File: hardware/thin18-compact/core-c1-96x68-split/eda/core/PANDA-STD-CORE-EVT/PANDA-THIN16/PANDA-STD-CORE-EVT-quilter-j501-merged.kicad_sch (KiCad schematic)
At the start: 126 parts, among them J301 DF58-2P-1.2V(21), J501 104031-0811 / microSD, J502 SM02B-SRSS-TB, J503 TC2030-IDC-NL / DEBUG, J803 FH34SRJ-6S-0.5SH(50), SW201 SKSCLCE010, SW202 SKSCLCE010, U301 BQ27427YZFR, U302 RV-3028-C7, U402 TPS22916CYFPT, U403 TPS22916CYFPT, U404 TPS22916CYFPT, U405 TPS22916CYFPT, U501 ESP32-S3-WROOM-1U-N16R8, U502 MAX98357AETE+T, U503 QMI8658A, U601 XL9535, U901 SGM41513YTQF24G/TR, U902 SGM62125AXG/TR, U903 CW2217BAAD, U904 NS4168

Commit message: feat(hw): audit split stack and verify exact-part sourcing
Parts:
- J301: LCSC (none) -> C597951
- J501: LCSC (none) -> C585350
- R306: LCSC (none) -> C7467248
- R903, R904: LCSC (none) -> C2906981
- U501: LCSC (none) -> C3013946
- U903: LCSC (none) -> C5203993

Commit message: hw: correct prototype footprints and prepare Split-C1 JLC CAM handoff
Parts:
- C506, C513: LCSC (none) -> C22399626; MPN 0603B106K100NT -> CGA0603X7R106K100JT; Manufacturer FH (Fenghua Advanced) -> HRE
- L402: footprint panda-standard:L402_2U2_ENVELOPE -> panda-standard:XGL4015_Coilcraft

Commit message: hw: apply reviewed domestic ECOs and gate incomplete Split-C1 orders
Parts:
- added C516: 1u / U403 VOUT, Capacitor_SMD:C_0603_1608Metric, symbol Device:C
- R201: LCSC C23189 -> C99891; MPN 0603WAF5601T5E -> RS-03K5601FT; Manufacturer UNI-ROYAL -> FH (Fenghua Advanced)
- R204: LCSC C22765 -> C118396; MPN 0603WAF1201T5E -> RS-03K1201FT; Manufacturer UNI-ROYAL -> FH (Fenghua Advanced)
- R303, R510, R511, R512, R513, R523, R524, R525, R526, R527, R528, R600: LCSC C25744 -> C140215; MPN 0402WGF1002TCE -> RC-02K1002FT; Manufacturer UNI-ROYAL -> FH (Fenghua Advanced)
- R501, R502, R507, R604, R605, R606, R607, R608, R609, R610, R611, R612: LCSC C25741 -> C140219; MPN 0402WGF1003TCE -> RC-02K1003FT; Manufacturer UNI-ROYAL -> FH (Fenghua Advanced)
- R508, R509, R514, R515, R516: LCSC C17477 -> C132364; MPN 0805W8F0000T5E -> RS-05000FT; Manufacturer UNI-ROYAL -> FH (Fenghua Advanced)
- R517, R518, R519, R520, R521, R522: LCSC C21189 -> C136582; MPN 0603WAF0000T5E -> RS-03000FT; Manufacturer UNI-ROYAL -> FH (Fenghua Advanced)
- R613, R614: LCSC C25879 -> C140192; MPN 0402WGF2201TCE -> RC-02K2201FT; Manufacturer UNI-ROYAL -> FH (Fenghua Advanced)
- U402, U403, U404, U405: value TPS22916CYFPT -> SGM2578SDYG/TR; footprint panda-standard:TPS22916CYFPT_YFP0004 -> panda-standard:SGM2578SD_WLCSP_09x09_P05; symbol panda-standard:TPS22916CYFPT -> panda-standard:SGM2578SDYG_TR; LCSC C2680456 -> (none); MPN TPS22916CYFPT -> SGM2578SDYG/TR; Manufacturer Texas Instruments -> SGMICRO
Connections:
- net 3V3_TOUCH_SW: now also C516.1
- net GND: now also C516.2

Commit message: hw: apply domestic wire, FPC and inductor ECOs with replay guards
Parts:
- J502: value SM02B-SRSS-TB -> HC-1.0-2PWT BTL; footprint Connector_JST:JST_SH_SM02B-SRSS-TB_1x02-1MP_P1.00mm_Horizontal -> panda-standard:HCTL_HC10_2PWT; LCSC C160402 -> C2845361; MPN SM02B-SRSS-TB(LF)(SN) -> HC-1.0-2PWT; Manufacturer JST -> HCTL
- J803: value FH34SRJ-6S-0.5SH(50) -> X05A10H06G; footprint PandaDomestic:FH34SRJ-6S-0.5SH_50 -> panda-standard:XKB_X05A10H06G_A2; LCSC C224194 -> C528032; MPN FH34SRJ-6S-0.5SH(50) -> X05A10H06G; Manufacturer Hirose -> XKB Connection; Qualification Exact C224194 land pattern imported; FPC orientation and ph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 -> Manufacturer X05A10HXX p2 A2, ECN-P-2026011502 dated2026-01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
- L401: value 0.47uH / M0-PENDING -> 0.47uH / SGM62125; footprint panda-standard:L401_XFL4015_ENVELOPE -> panda-standard:Sunlord_MWSA0402_R47; LCSC C18221164 -> C6331050; MPN XFL4015-471MEC -> MWSA0402S-R47MT; Manufacturer Coilcraft -> Sunlord
- L402: value 2.2u / BQ buck -> 1uH / SGM41513 buck; footprint panda-standard:XGL4015_Coilcraft -> panda-standard:Sunlord_MWSA0402_1R0B01; MPN XGL4015-222MEC -> MWSA0402S-1R0MTB01; Manufacturer Coilcraft -> Sunlord

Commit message: hw: replace side buttons with XKB A1 no-post switches
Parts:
- SW201, SW202: value SKSCLCE010 -> TS-1186E-B-B; footprint panda-standard:SW_Alps_SKSCLCE010 -> panda-standard:XKB_TS1186E_BB_A1; LCSC C139799 -> C2885153; MPN SKSCLCE010 -> TS-1186E-B-B; Manufacturer ALPSALPINE -> XKB Connection

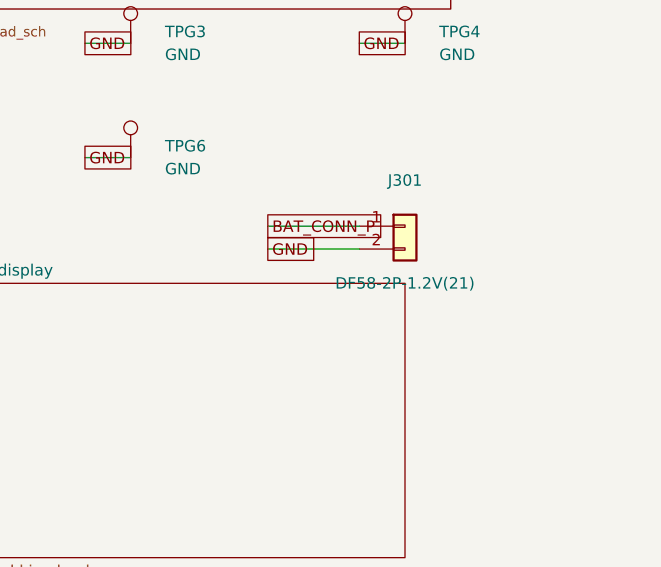
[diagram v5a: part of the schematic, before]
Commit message: hardware: close three imported Split-C1 refs and two SMT maps
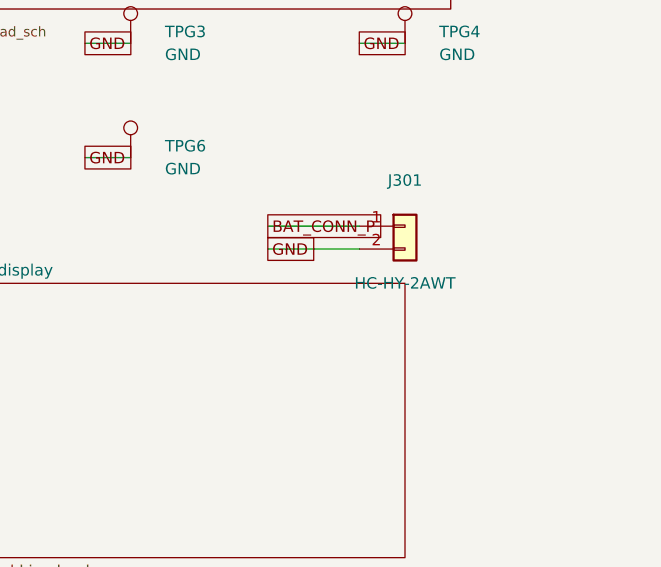
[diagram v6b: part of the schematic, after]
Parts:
- J301: value DF58-2P-1.2V(21) -> HC-HY-2AWT; footprint panda-battery:Hirose_DF58-2P-1.2V_1x02_P1.2mm_Vertical -> panda-standard:HCTL_HC_HY_2AWT; LCSC C597951 -> C2845705; MPN DF58-2P-1.2V(21) -> HC-HY-2AWT; Manufacturer Hirose -> HCTL

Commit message: hw: apply XUNPU microSD and reviewed Sunlord MT inductor ECOs
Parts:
- J501: value 104031-0811 / microSD -> TF-122-CCP9 / microSD; footprint Connector_Card:microSD_HC_Molex_104031-0811 -> panda-standard:XUNPU_TF_122_CCP9; symbol Connector:Micro_SD_Card_Det2 -> panda-standard:XUNPU_TF_122_CCP9; LCSC C585350 -> C41347844; MPN 104031-0811 -> TF-122-CCP9; Manufacturer Molex -> XUNPU
- L402: footprint panda-standard:Sunlord_MWSA0402_1R0B01 -> panda-standard:Sunlord_MWSA0402_1R0; LCSC (none) -> C408332; MPN MWSA0402S-1R0MTB01 -> MWSA0402S-1R0MT

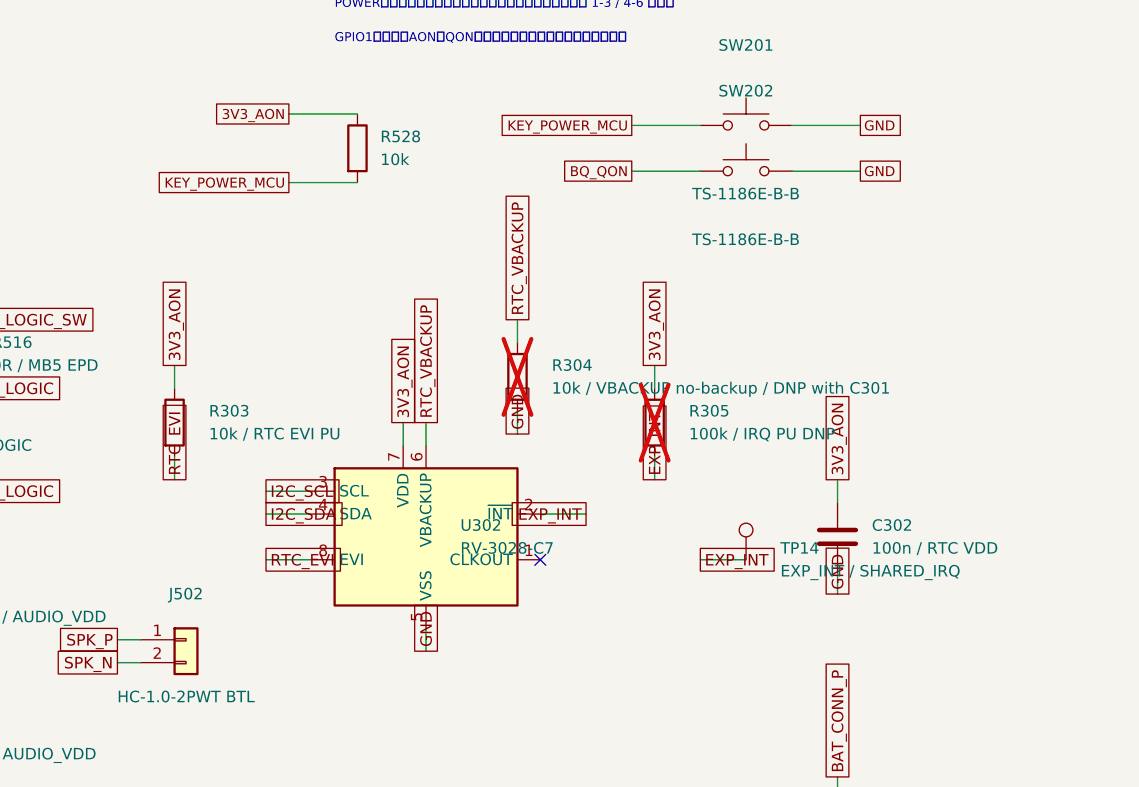
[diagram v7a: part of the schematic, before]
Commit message: hw: complete Split-C1 domestic RTC backup and EPD MOS ECO
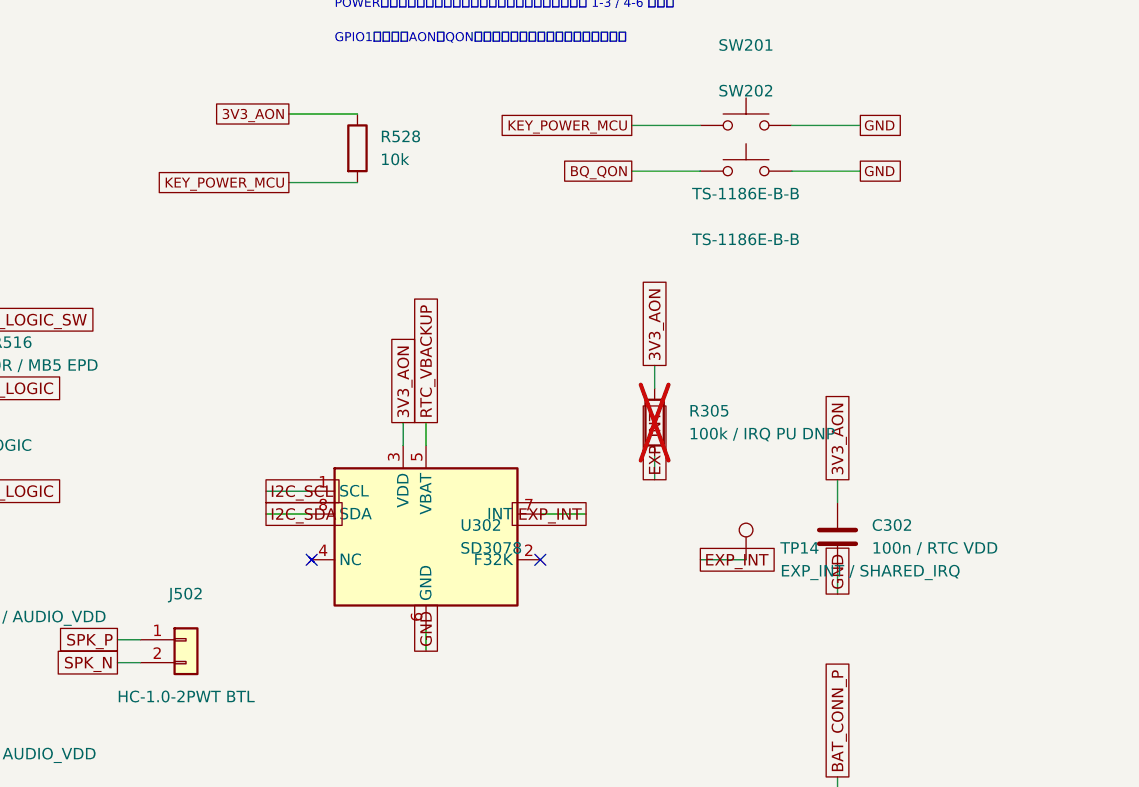
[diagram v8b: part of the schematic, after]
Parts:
- removed R303: 10k / RTC EVI PU, Resistor_SMD:R_0402_1005Metric, symbol Device:R
- removed R304: 10k / VBACKUP no-backup / DNP with C301, Resistor_SMD:R_0402_1005Metric, symbol Device:R
- U302: value RV-3028-C7 -> SD3078; footprint Package_SON:MicroCrystal_C7_SON-8_1.5x3.2mm_P0.9mm -> panda-standard:WAVE_SD3078_SOP8_208mil; symbol Timer_RTC:RV-3028-C7 -> panda-standard:SD3078; LCSC C3304278 -> C916255; MPN RV-3028-C7-32.768KHZ-1PPM-TA-QA -> SD3078; Manufacturer Micro Crystal -> WAVE
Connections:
- net RTC_EVI is gone; now on net I2C_SDA: U302.8 (SDA)
- net 3V3_AON: now also U302.3 (VDD); no longer U302.7 (VDD)
- net EXP_INT: now also U302.7 (INT); no longer U302.2 (~{INT})
- net GND: now also U302.6 (GND); no longer U302.5 (VSS)
- net I2C_SCL: now also U302.1 (SCL); no longer U302.3 (SCL)
- net I2C_SDA: no longer U302.4 (SDA)
- net RTC_VBACKUP: now also U302.5 (VBAT); no longer U302.6 (VBACKUP)
- no-connect marks 17 -> 18
